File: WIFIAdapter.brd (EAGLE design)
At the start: 25.8 x 44.7 mm, 17 parts

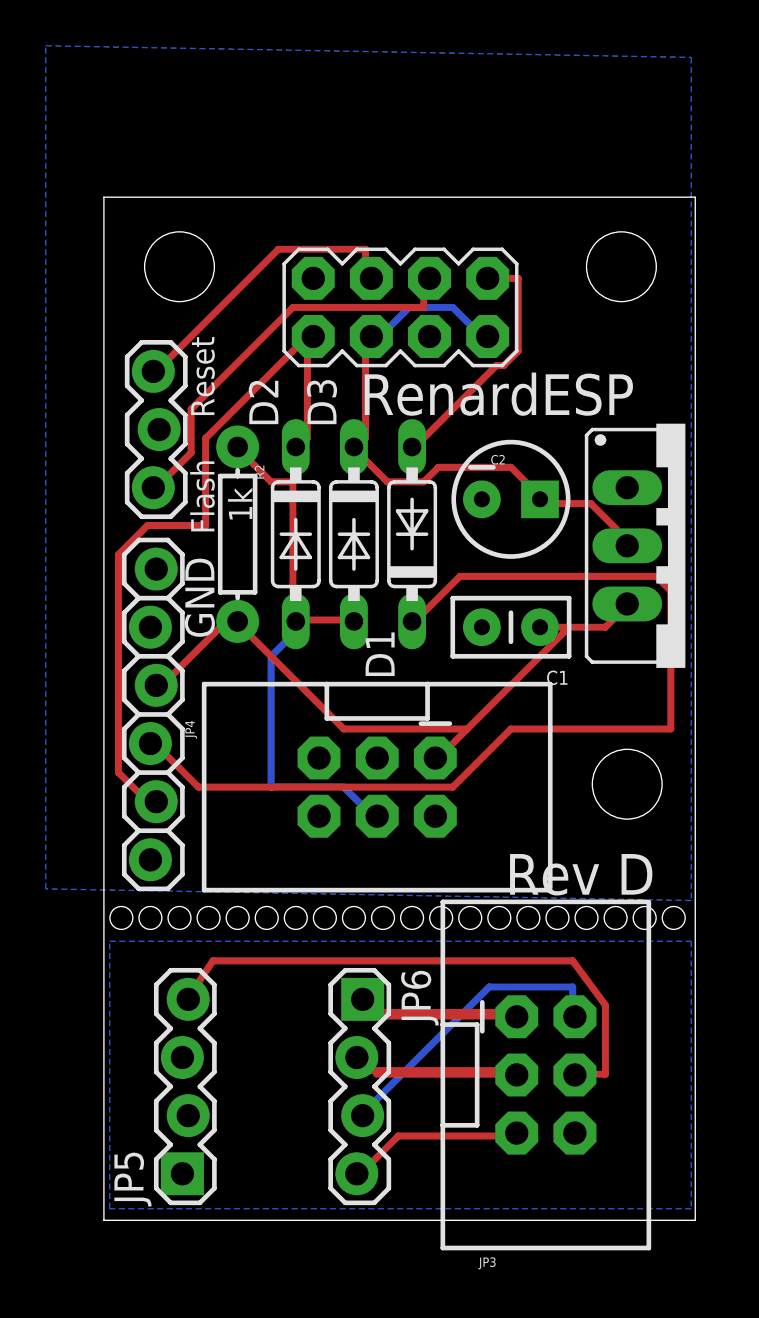
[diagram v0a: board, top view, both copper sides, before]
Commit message: Processed for SeeedStudo PCB service
Includes CAM files for Seeed
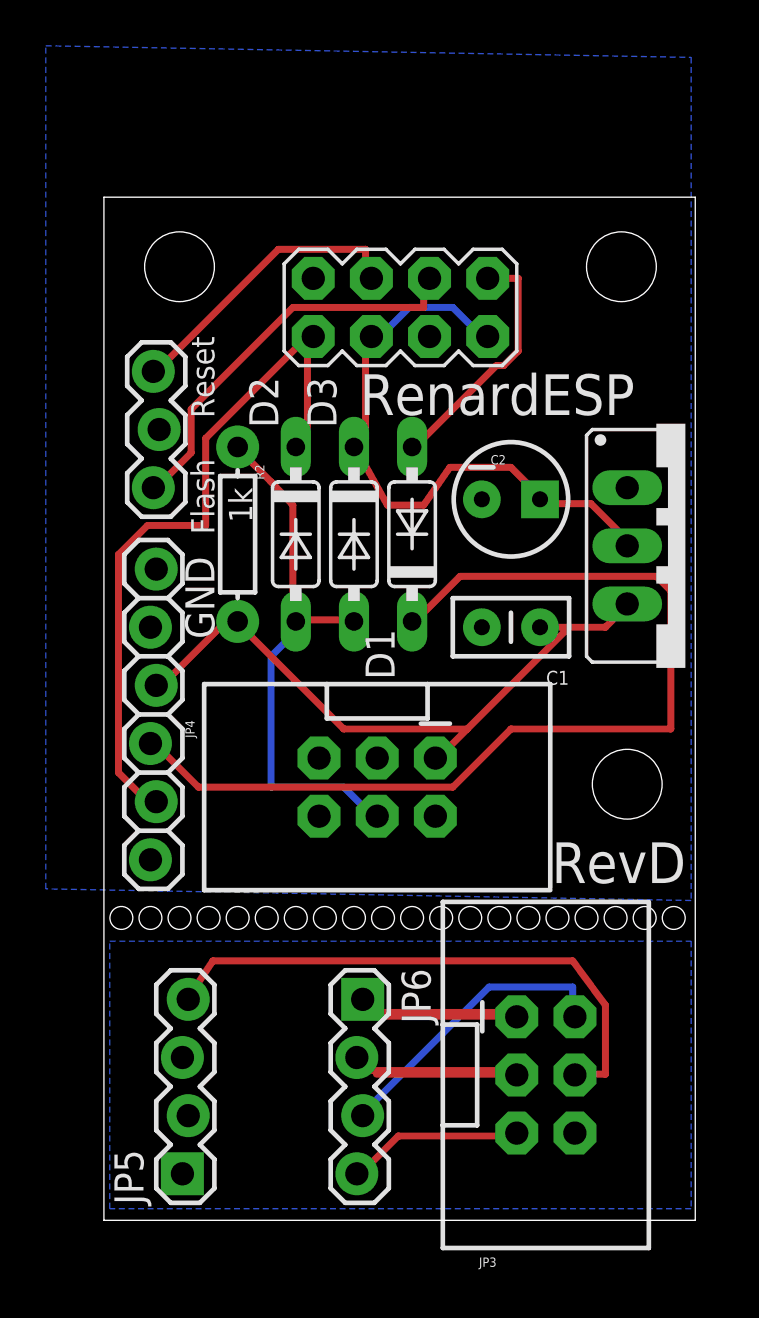
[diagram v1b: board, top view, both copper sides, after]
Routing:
- net 3.3V: track 26.1 -> 27.5 mm
- net N$11: track 24.6 -> 24.1 mm
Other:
- board text added: "RevD"
- board text removed: "Rev D"
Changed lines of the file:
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@@
 <text x="44.196" y="44.704" size="1.016" layer="25" rot="R90">Reset</text>
 <text x="44.196" y="39.624" size="1.016" layer="25" rot="R90">Flash</text>
-<text x="56.896" y="23.876" size="1.778" layer="25">Rev D</text>
+<text x="58.928" y="24.384" size="1.778" layer="25">RevD</text>
 </plain>
 <attributes>
@@
 </class>
 </classes>
-<designrules name="LaenPCBOrder">
+<designrules name="SeeedStudio_2layer_DRU_no_angle_20140221">
 <description language="de">&lt;b&gt;EAGLE Design Rules&lt;/b&gt;
 &lt;p&gt;
-Die Standard-Design-Rules sind so gewÃ¤hlt, dass sie fÃ¼r
+Die Standard-Design-Rules sind so gewählt, dass sie für
 die meisten Anwendungen passen. Sollte ihre Platine
 besondere Anforderungen haben, treffen Sie die erforderlichen
 Einstellungen hier und speichern die Design Rules unter
 einem neuen Namen ab.</description>
-<description language="en">&lt;b&gt;Laen's PCB Order Design Rules&lt;/b&gt;
+<description language="en">&lt;b&gt;EAGLE Design Rules&lt;/b&gt;
 &lt;p&gt;
-Please make sure your boards conform to these design rules.</description>
+The default Design Rules have been set to cover
+a wide range of applications. Your particular design
+may have different requirements, so please make the
+necessary adjustments and save your customized
+design rules under a new name.</description>
+<description language="zh">&lt;b&gt;Seeed Studio EAGLE Design Rules&lt;/b&gt;
+</description>
 <param name="layerSetup" value="(1*16)"/>
-<param name="mtCopper" value="0.0356mm 0.0356mm 0.0356mm 0.0356mm 0.0356mm 0.0356mm 0.0356mm 0.0356mm 0.0356mm 0.0356mm 0.0356mm 0.0356mm 0.0356mm 0.0356mm 0.0356mm 0.0356mm"/>
-<param name="mtIsolate" value="1.5011mm 0.1499mm 0.2007mm 0.1499mm 0.2007mm 0.1499mm 0.2007mm 0.1499mm 0.2007mm 0.1499mm 0.2007mm 0.1499mm 0.2007mm 0.1499mm 0.2007mm"/>
+<param name="mtCopper" value="0.035mm 0.0175mm 0.035mm 0.035mm 0.035mm 0.035mm 0.035mm 0.035mm 0.035mm 0.035mm 0.035mm 0.035mm 0.035mm 0.035mm 0.0175mm 0.035mm"/>
+<param name="mtIsolate" value="1.5mm 1.1mm 0.2mm 0.15mm 0.2mm 0.15mm 0.2mm 0.15mm 0.2mm 0.15mm 0.2mm 0.15mm 0.2mm 0.15mm 0.2mm"/>
 <param name="mdWireWire" value="6mil"/>
 <param name="mdWirePad" value="6mil"/>
@@
 <param name="mdPadVia" value="6mil"/>
 <param name="mdViaVia" value="6mil"/>
-<param name="mdSmdPad" value="6mil"/>
-<param name="mdSmdVia" value="6mil"/>
-<param name="mdSmdSmd" value="6mil"/>
+<param name="mdSmdPad" value="0mil"/>
+<param name="mdSmdVia" value="0mil"/>
+<param name="mdSmdSmd" value="0mil"/>
 <param name="mdViaViaSameLayer" value="8mil"/>
 <param name="mnLayersViaInSmd" value="2"/>
-<param name="mdCopperDimension" value="15mil"/>
-<param name="mdDrill" value="6mil"/>
+<param name="mdCopperDimension" value="10mil"/>
+<param name="mdDrill" value="10mil"/>
 <param name="mdSmdStop" value="0mil"/>
 <param name="msWidth" value="6mil"/>
-<param name="msDrill" value="13mil"/>
-<param name="msMicroVia" value="13mil"/>
+<param name="msDrill" value="12mil"/>
+<param name="msMicroVia" value="12mil"/>
 <param name="msBlindViaRatio" value="0.5"/>
 <param name="rvPadTop" value="0.25"/>
@@
 <param name="rvMicroViaOuter" value="0.25"/>
 <param name="rvMicroViaInner" value="0.25"/>
-<param name="rlMinPadTop" value="7mil"/>
+<param name="rlMinPadTop" value="10mil"/>
 <param name="rlMaxPadTop" value="20mil"/>
-<param name="rlMinPadInner" value="7mil"/>
+<param name="rlMinPadInner" value="10mil"/>
 <param name="rlMaxPadInner" value="20mil"/>
-<param name="rlMinPadBottom" value="7mil"/>
+<param name="rlMinPadBottom" value="10mil"/>
 <param name="rlMaxPadBottom" value="20mil"/>
-<param name="rlMinViaOuter" value="7mil"/>
+<param name="rlMinViaOuter" value="6mil"/>
 <param name="rlMaxViaOuter" value="20mil"/>
-<param name="rlMinViaInner" value="7mil"/>
+<param name="rlMinViaInner" value="6mil"/>
 <param name="rlMaxViaInner" value="20mil"/>
 <param name="rlMinMicroViaOuter" value="4mil"/>
@@
 <param name="psTop" value="-1"/>
 <param name="psBottom" value="-1"/>
-<param name="psFirst" value="-1"/>
+<param name="psFirst" value="0"/>
 <param name="psElongationLong" value="100"/>
 <param name="psElongationOffset" value="100"/>
 <param name="mvStopFrame" value="1"/>
 <param name="mvCreamFrame" value="0"/>
-<param name="mlMinStopFrame" value="3mil"/>
-<param name="mlMaxStopFrame" value="3mil"/>
+<param name="mlMinStopFrame" value="2mil"/>
+<param name="mlMaxStopFrame" value="2mil"/>
 <param name="mlMinCreamFrame" value="0mil"/>
 <param name="mlMaxCreamFrame" value="0mil"/>
-<param name="mlViaStopLimit" value="0mil"/>
+<param name="mlViaStopLimit" value="100mil"/>
 <param name="srRoundness" value="0"/>
 <param name="srMinRoundness" value="0mil"/>
@@
 <param name="checkAngle" value="0"/>
 <param name="checkFont" value="1"/>
-<param name="checkRestrict" value="1"/>
+<param name="checkRestrict" value="0"/>
 <param name="useDiameter" value="13"/>
 <param name="maxErrors" value="50"/>
@@
 <wire x1="58.42" y1="40.9575" x2="58.42" y2="41.148" width="0.3048" layer="1"/>
 <wire x1="57.15" y1="42.545" x2="58.42" y2="41.275" width="0.3048" layer="1"/>
-<wire x1="53.975" y1="42.545" x2="57.15" y2="42.545" width="0.3048" layer="1"/>
-<wire x1="53.34" y1="41.91" x2="53.975" y2="42.545" width="0.3048" layer="1"/>
-<wire x1="51.7525" y1="41.91" x2="53.34" y2="41.91" width="0.3048" layer="1"/>
-<wire x1="50.4825" y1="43.18" x2="51.7525" y2="41.91" width="0.3048" layer="1"/>
+<wire x1="54.483" y1="42.545" x2="57.15" y2="42.545" width="0.3048" layer="1"/>
+<wire x1="53.34" y1="40.894" x2="54.483" y2="42.545" width="0.3048" layer="1"/>
+<wire x1="51.7525" y1="40.894" x2="53.34" y2="40.894" width="0.3048" layer="1"/>
+<wire x1="50.4825" y1="43.18" x2="51.7525" y2="40.894" width="0.3048" layer="1"/>
 <wire x1="58.42" y1="41.275" x2="58.42" y2="41.148" width="0.3048" layer="1"/>
 <wire x1="50.4825" y1="43.18" x2="50.292" y2="43.434" width="0.3048" layer="1"/>
@@
 <wire x1="47.9425" y1="35.8775" x2="47.752" y2="35.814" width="0.3048" layer="1"/>
 <wire x1="50.165" y1="35.8775" x2="50.292" y2="35.814" width="0.3048" layer="1"/>
-<wire x1="47.625" y1="41.91" x2="47.625" y2="35.8775" width="0.3048" layer="1"/>
-<wire x1="46.6725" y1="41.91" x2="47.625" y2="41.91" width="0.3048" layer="1"/>
+<wire x1="47.625" y1="40.894" x2="47.625" y2="35.8775" width="0.3048" layer="1"/>
+<wire x1="46.6725" y1="41.91" x2="47.625" y2="40.894" width="0.3048" layer="1"/>
 <wire x1="45.4025" y1="43.18" x2="46.6725" y2="41.91" width="0.3048" layer="1"/>
 <wire x1="47.625" y1="35.8775" x2="47.752" y2="35.814" width="0.3048" layer="1"/>

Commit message: RevE with 8 pin DIP adapter
Trade the break away PCB adapter for a COTS ribbon cable DIP adapter.
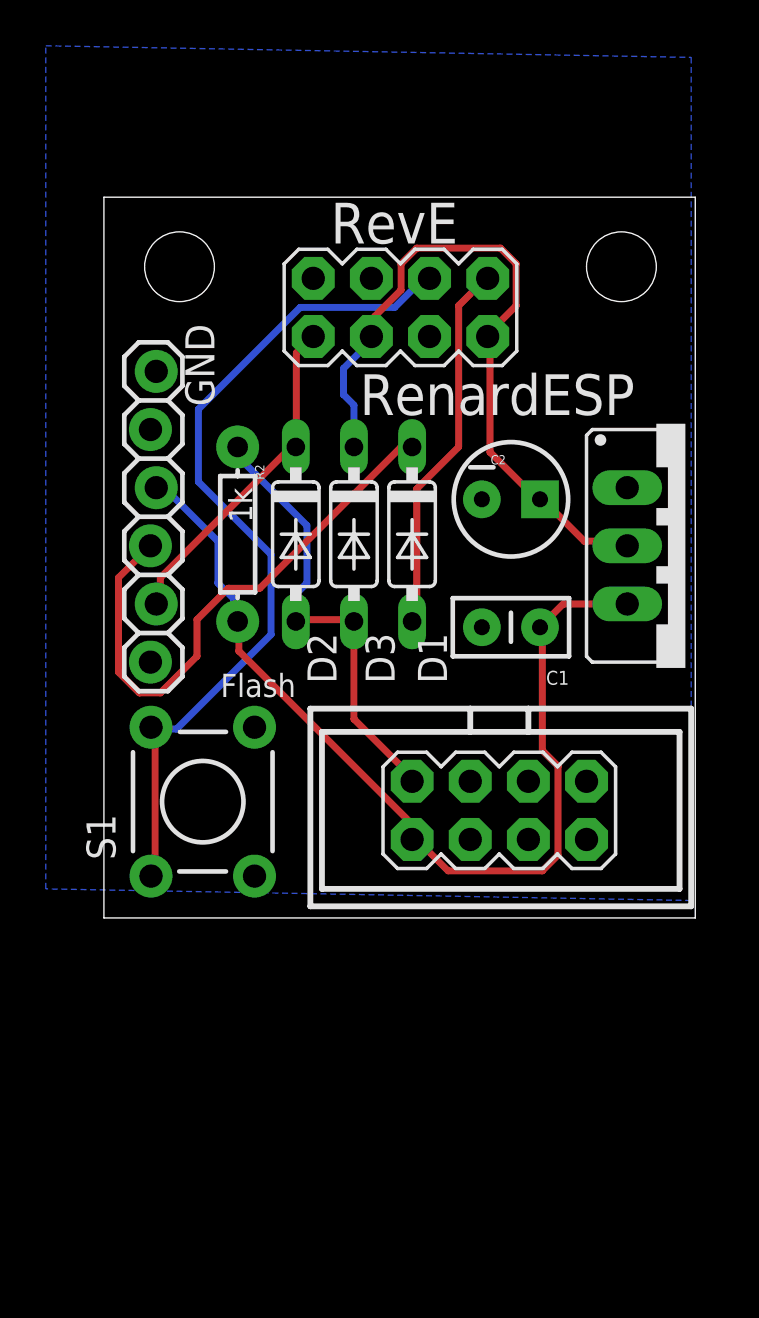
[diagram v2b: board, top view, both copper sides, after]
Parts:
- removed JP3, JP4: (no value), SparkFun-Connectors:2X3-SHROUDED
- removed JP5, JP6: (no value), SparkFun-Connectors:1X04_LOCK
- removed JP7: (no value), SparkFun-Connectors:1X03_LOCK
- removed STANDOFF3: STAND-OFFTIGHT, SparkFun-Electromechanical:STAND-OFF-TIGHT
- added S1: (no value), SparkFun-Electromechanical:TACTILE-PTH
- added U$1: M04X2, SparkFun-Connectors:2X4
- moved JP1 8.64 mm to (41.4, 34.0)
- turned D1 to 270 degrees
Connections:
- net N$1 renamed TX
- net N$2 renamed RX
- removed net N$10: JP3.5, JP6.4
- removed net N$12: JP3.4, JP5.4
- removed net N$4: JP3.1, JP6.1
- removed net N$5: JP3.2, JP6.3
- removed net N$6: JP7.3, U$2.4
- removed net N$9: JP3.3, JP6.2
- net 5V: now also U$1.1; no longer JP4.1
- net GND: now also S1.3, S1.4, U$1.7; no longer JP4.5, JP7.2
- net N$11: now also U$1.2; no longer JP4.4
- net N$7: now also S1.1, S1.2; no longer JP7.1
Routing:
- net N$12: track 24.7 -> 0.00 mm
- net N$7: track 17.7 -> 37.4 mm
- net N$8: track 43.0 -> 24.7 mm
- net TX: track 31.5 -> 14.8 mm
- net N$9: track 13.5 -> 0.00 mm
- net N$4: track 13.2 -> 0.00 mm
- net N$5: track 13.1 -> 0.00 mm
- net N$6: track 13.0 -> 0.00 mm
- net 5V: track 29.2 -> 42.0 mm
- net N$10: track 8.00 -> 0.00 mm
- net RX: track 10.9 -> 16.4 mm
- net N$11: track 24.1 -> 19.8 mm
- net 3.3V: track 27.5 -> 31.6 mm
- removed copper zone on layer 16, net N$15
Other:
- board size 25.8 x 44.7 mm -> 25.8 x 31.5 mm
- board text added: "RevE"
- board text removed: "Reset"
- board text removed: "RevD"
